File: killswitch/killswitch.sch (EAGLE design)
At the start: 27 parts, among them U1 CD4012BPWR, U2 MMBT2222ALT1G, U3 MMBT3906LT1G

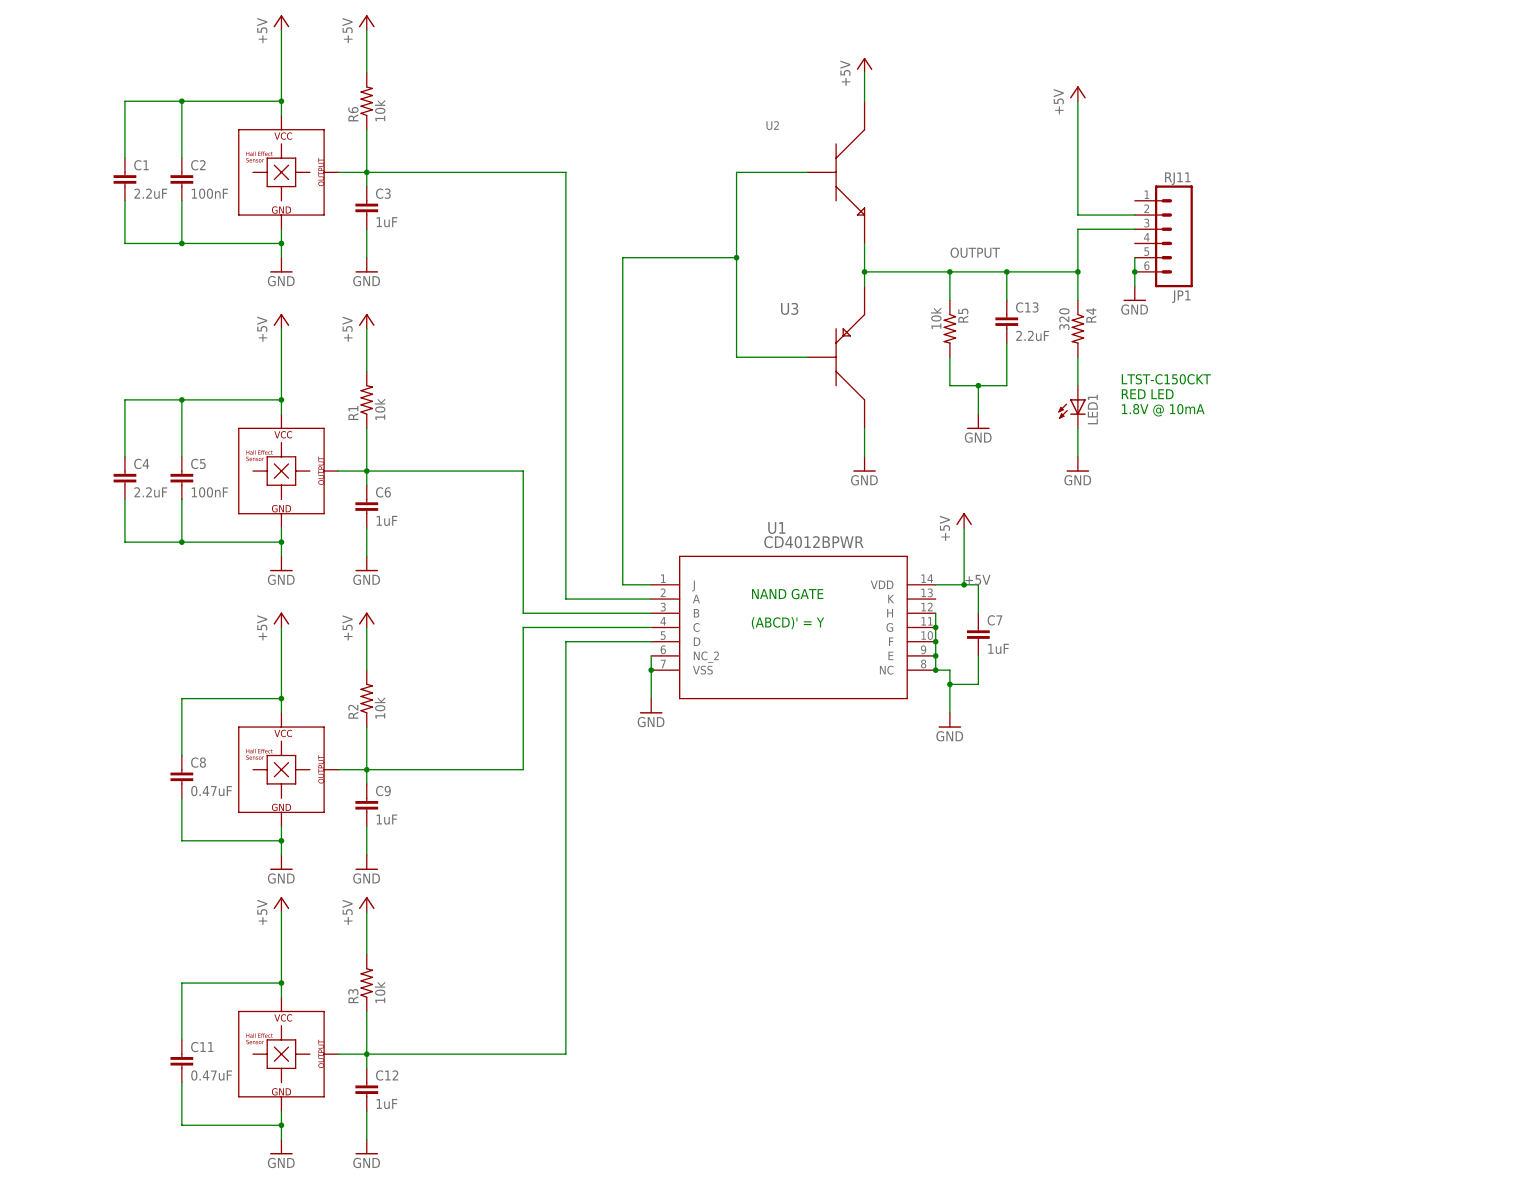
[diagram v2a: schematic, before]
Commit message: Using MOS output buffer
-also added EAGLE libraries
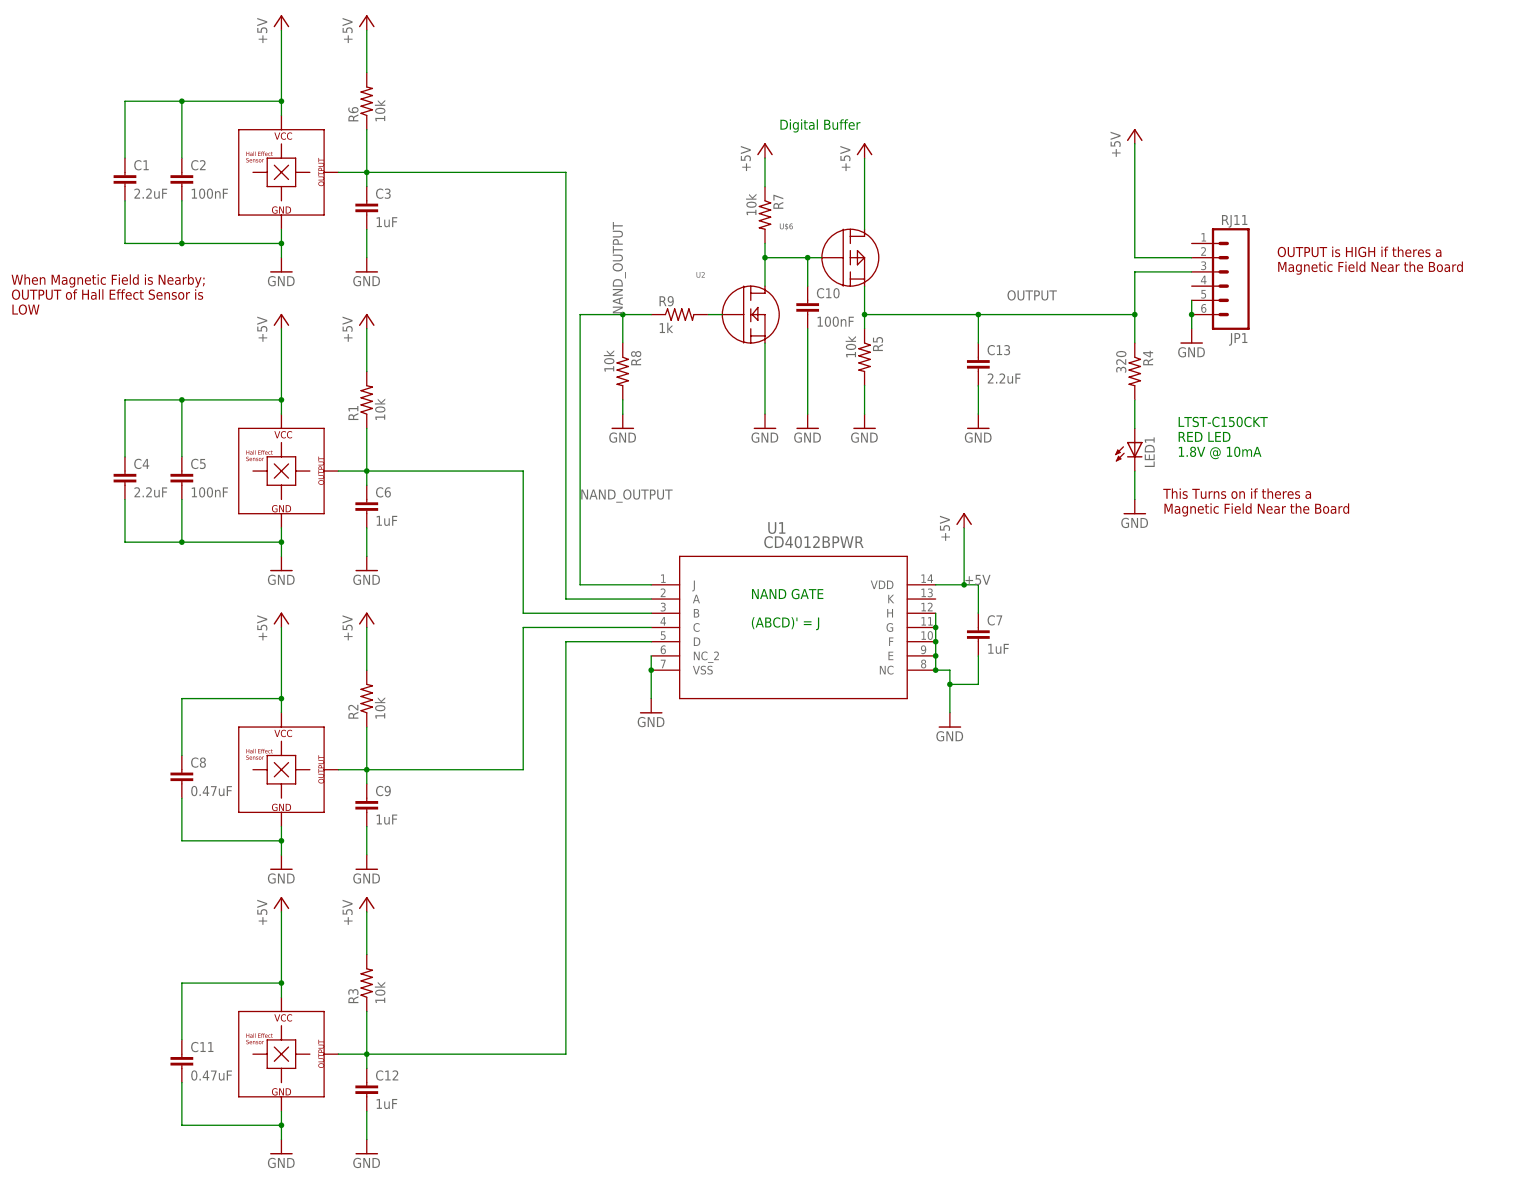
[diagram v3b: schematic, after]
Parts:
- removed U3: MMBT3906LT1G, KillSwitch:MMBT3906LT1G
- added C10: 100nF, resistor:C-EUC0805
- added R7, R8: 10k, resistor:R-US_R0805
- added R9: 1k, resistor:R-US_R0805
- added U$6: DMP2066LDM-7, KillSwitch:DMP2066LDM-7
- U2: value MMBT2222ALT1G -> 2N7002-7-F; device KillSwitch:MMBT2222ALT1G -> KillSwitch:2N7002-7-F
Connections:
- removed net N$6: U1.J, U2.B, U3.B
- new net N$10: R9.2, U2.G
- new net N$9: C10.1, R7.2, U$6.GATE, U2.D
- new net NAND_OUTPUT: R8.1, R9.1, U1.J
- net +5V: now also R7.1; no longer U2.C
- net GND: now also C10.2, R8.2, U2.S; no longer U3.C
- net OUTPUT: now also U$6.SOURCE; no longer U2.E, U3.E
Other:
- note added: "(ABCD)' = J"
- note added: "Digital Buffer"
- note added: "OUTPUT is HIGH if theres a Magnetic Field Near the Board"
- note added: "This Turns on if theres a Magnetic Field Near the Board"
- note added: "When Magnetic Field is Nearby; OUTPUT of Hall Effect Sensor is LOW"
- note removed: "(ABCD)' = Y"
- moved on the sheet: C13, JP1, LED1, R4, R5

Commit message: Removed RJ11 and replaced with 3-pin Header
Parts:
- JP1: value RJ11 -> (none); device SparkFun-Connectors:RJ11-6PTH -> pinhead:PINHD-1X3
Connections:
- net +5V: now also JP1.1; no longer JP1.2
- net GND: now also JP1.3; no longer JP1.5, JP1.6
- net OUTPUT: now also JP1.2; no longer JP1.3
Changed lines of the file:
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@@
 <parts>
 <part name="GND1" library="supply1" library_urn="urn:adsk.eagle:library:371" deviceset="GND" device=""/>
-<part name="JP1" library="SparkFun-Connectors" deviceset="RJ11-6" device="PTH" value="RJ11"/>
 <part name="P+4" library="supply1" library_urn="urn:adsk.eagle:library:371" deviceset="+5V" device=""/>
 <part name="GND3" library="supply1" library_urn="urn:adsk.eagle:library:371" deviceset="GND" device=""/>
@@
 <part name="C10" library="resistor" library_urn="urn:adsk.eagle:library:348" deviceset="C-EU" device="C0805" package3d_urn="urn:adsk.eagle:package:26137/1" value="100nF"/>
 <part name="GND17" library="supply1" library_urn="urn:adsk.eagle:library:371" deviceset="GND" device=""/>
+<part name="JP1" library="pinhead" library_urn="urn:adsk.eagle:library:325" deviceset="PINHD-1X3" device="" package3d_urn="urn:adsk.eagle:package:22458/2"/>
 </parts>
 <sheets>
@@
 <instances>
 <instance part="GND1" gate="1" x="-27.94" y="35.56"/>
-<instance part="JP1" gate="G$1" x="139.7" y="35.56" rot="R180"/>
 <instance part="P+4" gate="1" x="124.46" y="60.96"/>
 <instance part="GND3" gate="1" x="134.62" y="22.86"/>
@@
 <instance part="C10" gate="G$1" x="66.04" y="30.48"/>
 <instance part="GND17" gate="1" x="66.04" y="7.62"/>
+<instance part="JP1" gate="A" x="139.7" y="35.56"/>
 </instances>
 <busses>
@@
 <segment>
 <pinref part="GND3" gate="1" pin="GND"/>
-<wire x1="134.62" y1="25.4" x2="134.62" y2="27.94" width="0.1524" layer="91"/>
-<pinref part="JP1" gate="G$1" pin="5"/>
-<wire x1="134.62" y1="27.94" x2="134.62" y2="30.48" width="0.1524" layer="91"/>
-<pinref part="JP1" gate="G$1" pin="6"/>
-<junction x="134.62" y="27.94"/>
+<wire x1="134.62" y1="25.4" x2="134.62" y2="33.02" width="0.1524" layer="91"/>
+<pinref part="JP1" gate="A" pin="3"/>
+<wire x1="134.62" y1="33.02" x2="137.16" y2="33.02" width="0.1524" layer="91"/>
 </segment>
 <segment>
@@
 <net name="+5V" class="0">
 <segment>
-<pinref part="JP1" gate="G$1" pin="2"/>
-<wire x1="134.62" y1="38.1" x2="124.46" y2="38.1" width="0.1524" layer="91"/>
+<wire x1="137.16" y1="38.1" x2="124.46" y2="38.1" width="0.1524" layer="91"/>
 <wire x1="124.46" y1="38.1" x2="124.46" y2="58.42" width="0.1524" layer="91"/>
 <pinref part="P+4" gate="1" pin="+5V"/>
+<pinref part="JP1" gate="A" pin="1"/>
 </segment>
 <segment>
@@
 <segment>
 <wire x1="124.46" y1="27.94" x2="124.46" y2="35.56" width="0.1524" layer="91"/>
-<pinref part="JP1" gate="G$1" pin="3"/>
-<wire x1="124.46" y1="35.56" x2="134.62" y2="35.56" width="0.1524" layer="91"/>
+<wire x1="124.46" y1="35.56" x2="137.16" y2="35.56" width="0.1524" layer="91"/>
 <label x="101.6" y="30.48" size="1.778" layer="95"/>
 <pinref part="R4" gate="G$1" pin="1"/>
@@
 <wire x1="96.52" y1="27.94" x2="96.52" y2="22.86" width="0.1524" layer="91"/>
 <junction x="96.52" y="27.94"/>
-</segment>
-</net>
+<pinref part="JP1" gate="A" pin="2"/>
+</segment>
+</net>

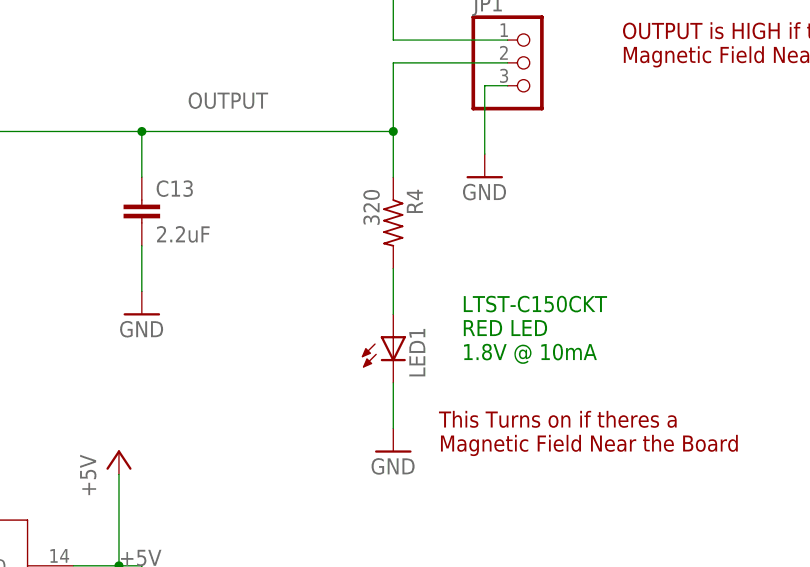
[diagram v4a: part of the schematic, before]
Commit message: Minor tweaks to traces.
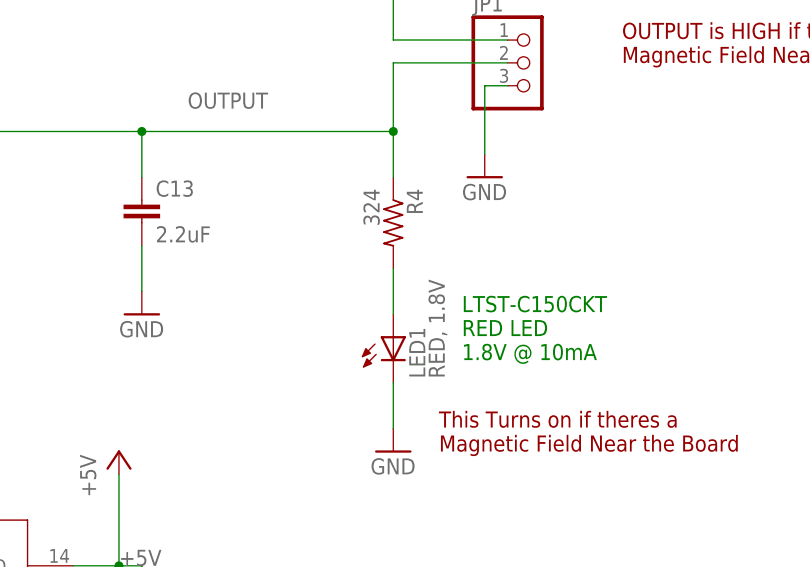
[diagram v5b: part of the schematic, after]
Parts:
- LED1: value (none) -> RED, 1.8V
- R4: value 320 -> 324
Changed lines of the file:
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@@
 <part name="GND13" library="supply1" library_urn="urn:adsk.eagle:library:371" deviceset="GND" device=""/>
 <part name="C7" library="resistor" library_urn="urn:adsk.eagle:library:348" deviceset="C-EU" device="C0603" package3d_urn="urn:adsk.eagle:package:26138/1" value="1uF"/>
-<part name="R4" library="resistor" library_urn="urn:adsk.eagle:library:348" deviceset="R-US_" device="R0805" package3d_urn="urn:adsk.eagle:package:26059/1" value="320"/>
-<part name="LED1" library="SparkFun (2015_10_14 22_27_04 UTC)" deviceset="LED" device="1206"/>
+<part name="R4" library="resistor" library_urn="urn:adsk.eagle:library:348" deviceset="R-US_" device="R0805" package3d_urn="urn:adsk.eagle:package:26059/1" value="324"/>
+<part name="LED1" library="SparkFun (2015_10_14 22_27_04 UTC)" deviceset="LED" device="1206" value="RED, 1.8V"/>
 <part name="GND14" library="supply1" library_urn="urn:adsk.eagle:library:371" deviceset="GND" device=""/>
 <part name="U1" library="KillSwitch" library_urn="urn:adsk.eagle:library:576207" deviceset="CD4012BPWR" device=""/>

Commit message: pMOS in schematic wasn't attached to 5V. Fixed that.
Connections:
- net +5V: now also U$6.DRAIN
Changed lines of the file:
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@@
 <wire x1="76.2" y1="43.18" x2="76.2" y2="55.88" width="0.1524" layer="91"/>
 <pinref part="P+11" gate="1" pin="+5V"/>
+<pinref part="U$6" gate="A" pin="DRAIN"/>
 </segment>
 <segment>

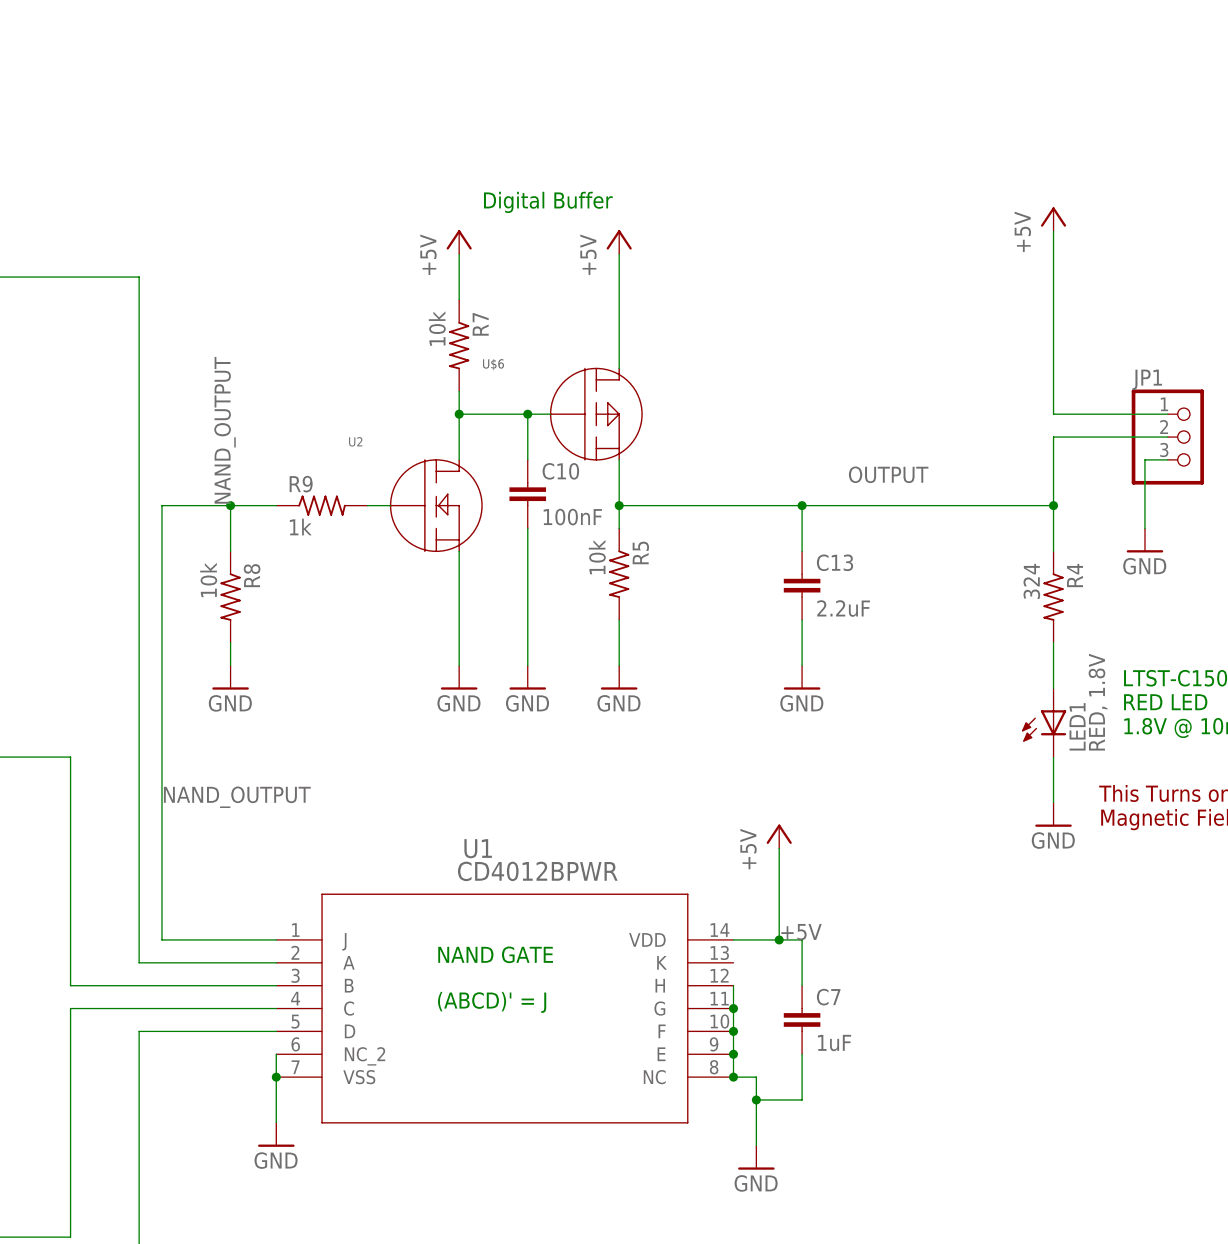
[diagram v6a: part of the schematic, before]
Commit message: Output wasnt pulling low. Using a push-pull buffer and an AND gate instead
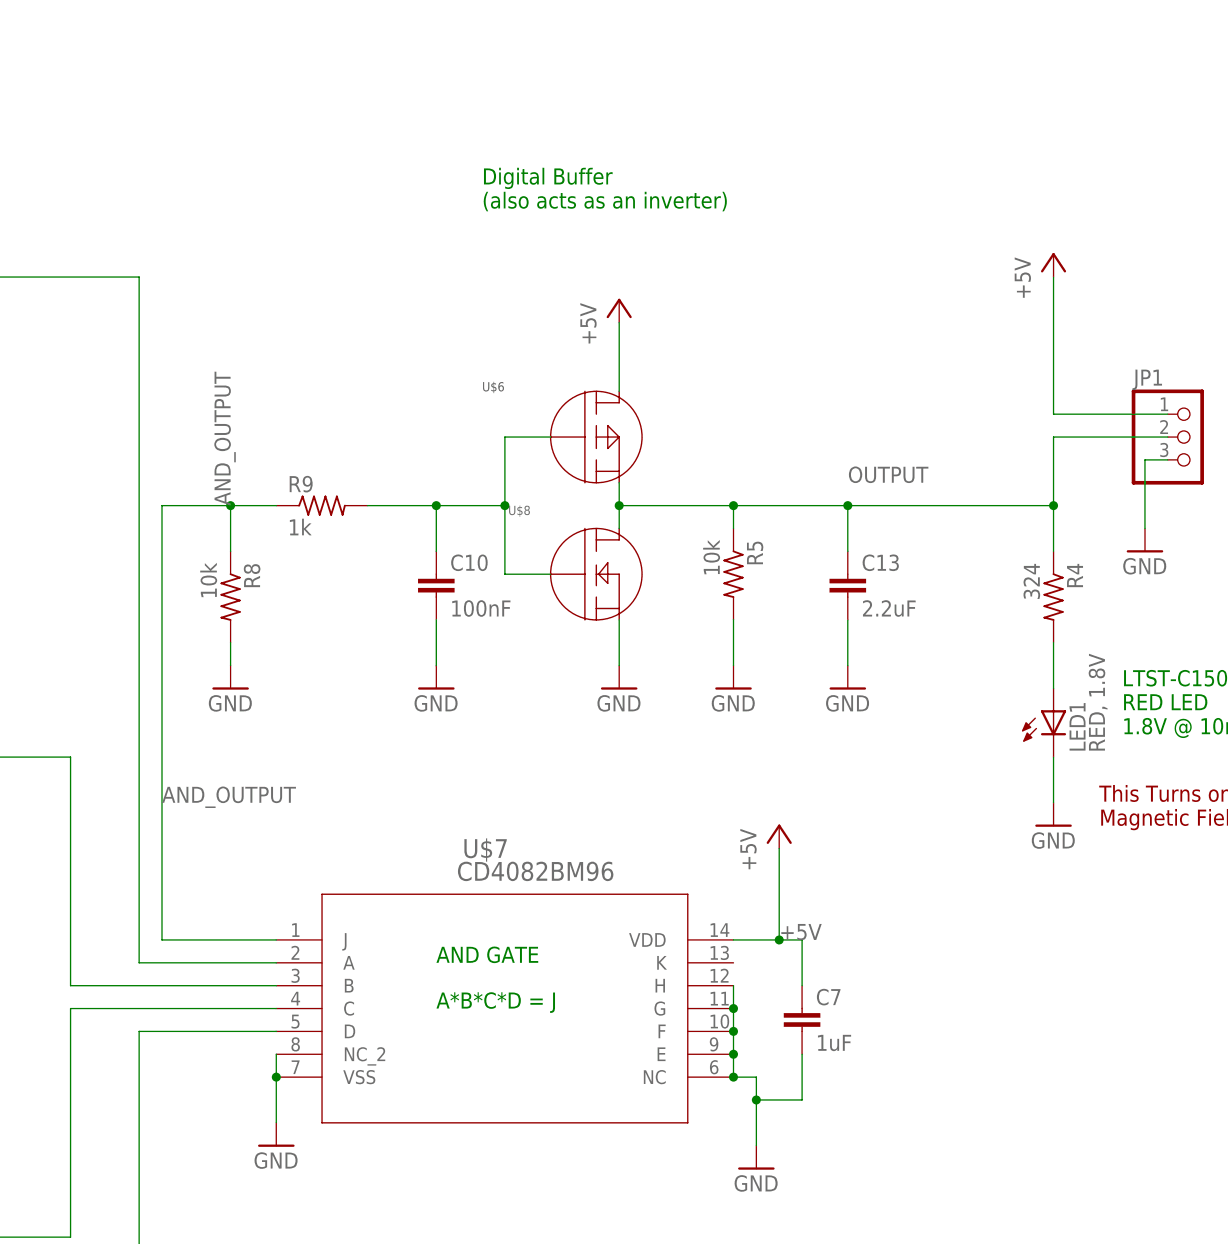
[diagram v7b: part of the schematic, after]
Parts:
- removed R7: 10k, resistor:R-US_R0805
- removed U1: CD4012BPWR, KillSwitch:CD4012BPWR
- removed U2: 2N7002-7-F, KillSwitch:2N7002-7-F
- added U$7: CD4082BM96, KillSwitch:CD4082BM96
- added U$8: IRLMS2002TRPBF, KillSwitch:IRLMS2002TRPBF
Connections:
- removed net N$9: C10.1, R7.2, U$6.GATE, U2.D
- removed net NAND_OUTPUT: R8.1, R9.1, U1.J
- new net AND_OUTPUT: R8.1, R9.1, U$7.J
- net +5V: now also U$7.VDD; no longer R7.1, U1.VDD
- net GND: now also U$7.E, U$7.F, U$7.G, U$7.H, U$7.NC, U$7.NC_2, U$7.VSS, U$8.S; no longer U1.E, U1.F, U1.G, U1.H, U1.NC, U1.NC_2, U1.VSS, U2.S
- net N$1: now also U$7.B; no longer U1.B
- net N$10: now also C10.1, U$6.GATE, U$8.G; no longer U2.G
- net N$2: now also U$7.C; no longer U1.C
- net N$3: now also U$7.D; no longer U1.D
- net N$5: now also U$7.A; no longer U1.A
- net OUTPUT: now also U$8.D
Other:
- note added: "A*B*C*D = J"
- note added: "AND GATE"
- note added: "Digital Buffer (also acts as an inverter)"
- note removed: "(ABCD)' = J"
- note removed: "Digital Buffer"
- note removed: "NAND GATE"
- moved on the sheet: C10, C13, R5, U$6
